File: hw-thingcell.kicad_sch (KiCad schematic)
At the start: 80 parts, among them J1 Conn_01x02_Pin, J2 GSM_ANT, J3 GNSS_ANT, J4 Conn_01x08_Pin, J5 SIM8060-6-0-14-00-A, K1 JRC-21F(4100), Q1 PMBT3904235, Q2 PMBT3904235, SW1 SW_Push, U1 ESP32-WROOM-32, U2 AP62301WU-7, U3 AP62301WU-7, U4 SIM868

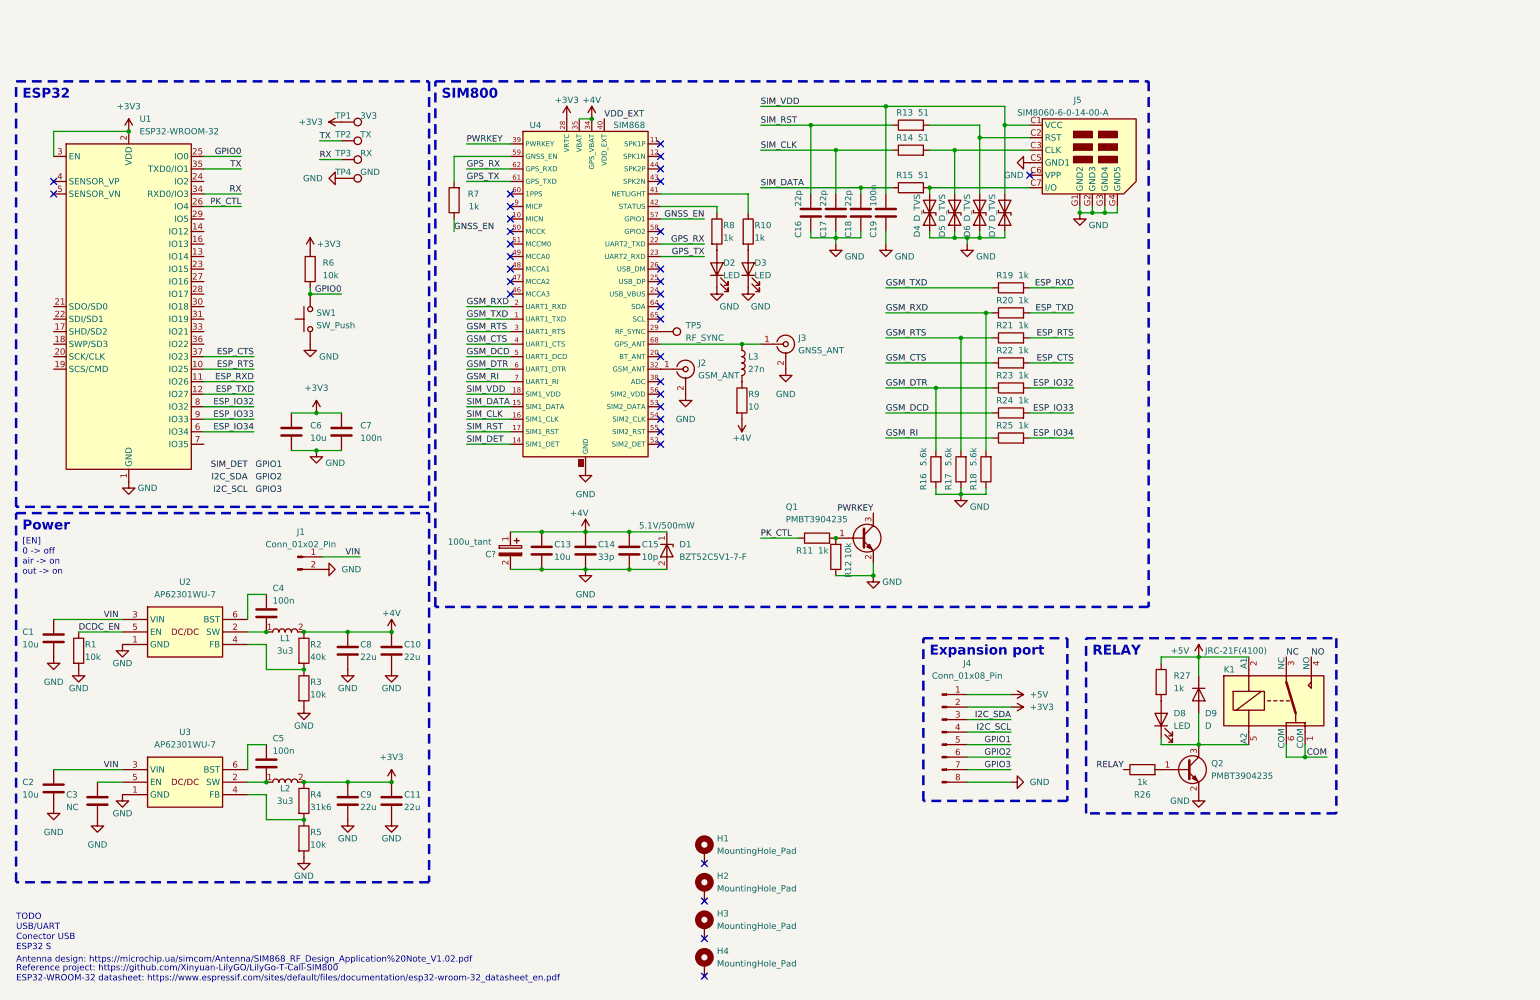
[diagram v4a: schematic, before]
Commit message: Add USB-UART and USB-C connector
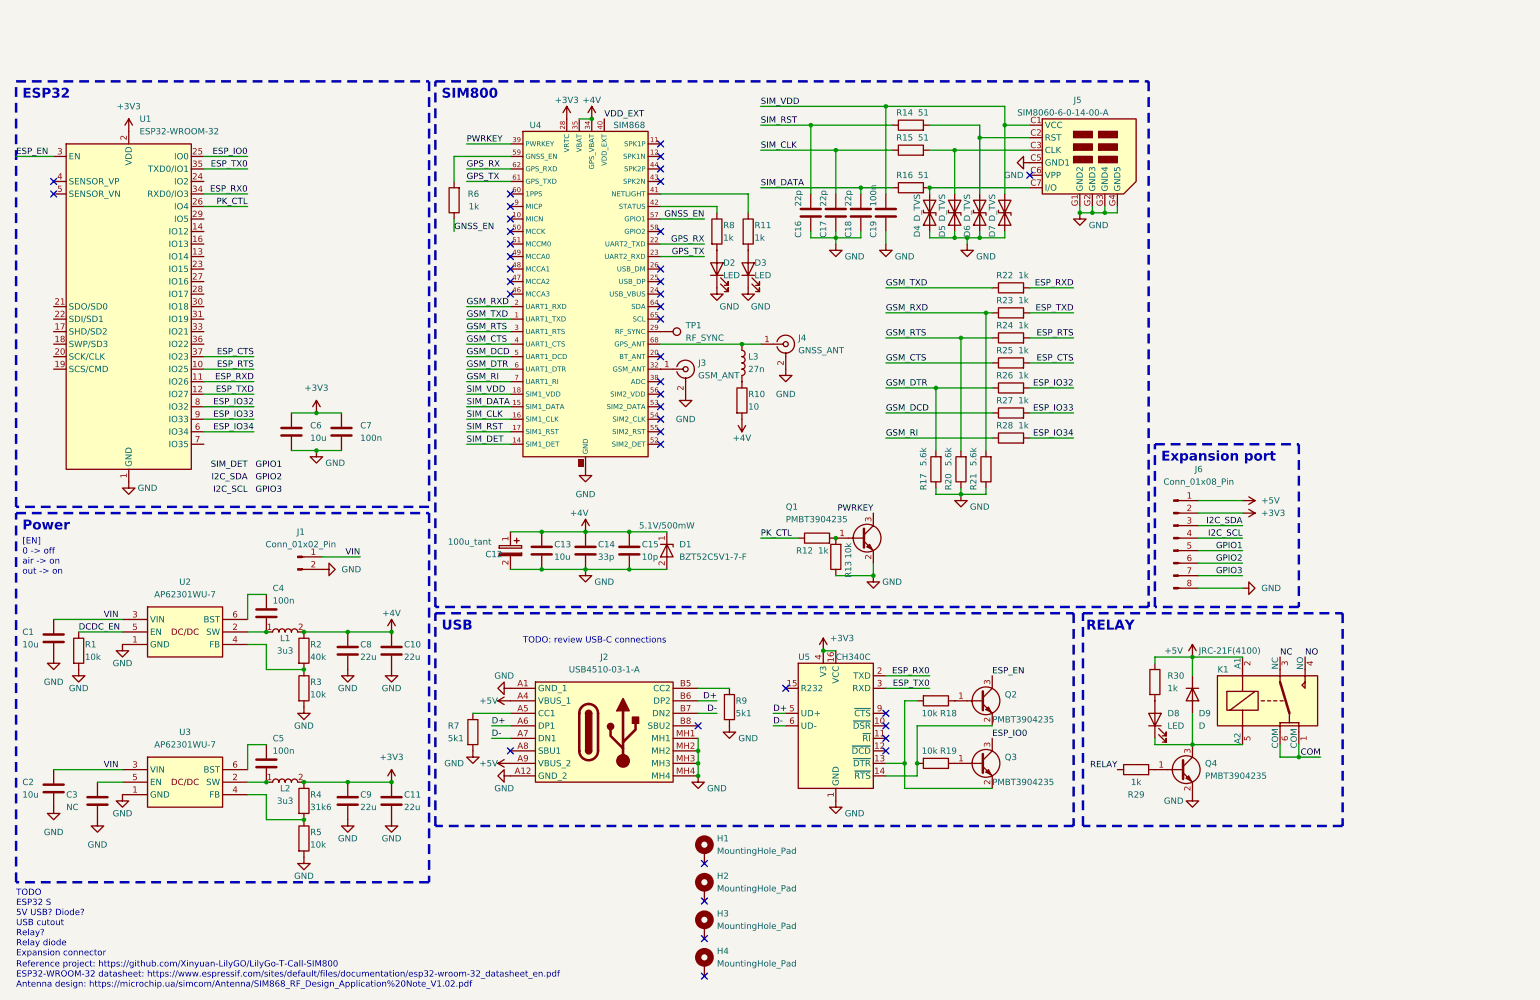
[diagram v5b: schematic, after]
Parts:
- removed R6: 10k, Resistor_SMD:R_0402_1005Metric, symbol Device:R
- removed SW1: SW_Push, symbol Switch:SW_Push
- removed TP1: 3V3, TestPoint:TestPoint_Pad_D1.0mm, symbol Connector:TestPoint
- removed TP2: TX, TestPoint:TestPoint_Pad_D1.0mm, symbol Connector:TestPoint
- removed TP3: RX, TestPoint:TestPoint_Pad_D1.0mm, symbol Connector:TestPoint
- removed TP4: GND, TestPoint:TestPoint_Pad_D1.0mm, symbol Connector:TestPoint
- added J2: USB4510-03-1-A, guille-lib:USB4510031A, symbol guille-lib:USB4510-03-1-A
- added Q2, Q3: PMBT3904235, Package_TO_SOT_SMD:SOT-23, symbol guille-lib:PMBT3904235
- added R18, R19: 10k, Resistor_SMD:R_0402_1005Metric, symbol Device:R
- added R7, R9: 5k1, Resistor_SMD:R_0402_1005Metric, symbol Device:R
- added U5: CH340C, Package_SO:SOIC-16_3.9x9.9mm_P1.27mm, symbol Interface_USB:CH340C
- gave numbers to parts that had none: 1
- renumbered J2 to J3, J3 to J4, J4 to J6, Q2 to Q4, R9 to R10, R10 to R11, R11 to R12, R12 to R13, R13 to R14, R14 to R15, R15 to R16, R16 to R17, R17 to R20, R18 to R21, R19 to R22, R20 to R23, R21 to R24, R22 to R25, R23 to R26, R24 to R27, R25 to R28, R26 to R29, R27 to R30, R7 to R6, TP5 to TP1
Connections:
- net +3V3: now also U5.16 (VCC), U5.4 (V3); no longer U1.3 (EN)
- net +5V: now also J2.A4 (VBUS_1), J2.A9 (VBUS_2)
- net GND: now also J2.A1 (GND_1), J2.A12 (GND_2), J2.MH1, J2.MH2, J2.MH3, J2.MH4, R7.2, R9.2, U5.1 (GND)
- net GPIO0 renamed ESP_IO0
- net ESP_IO0: now also Q3.3
- net RX renamed ESP_RX0
- net ESP_RX0: now also U5.2 (TXD)
- net TX renamed ESP_TX0
- net ESP_TX0: now also U5.3 (RXD)
- new net: Q3.2, R18.2, U5.13 (~{DTR})
- new net: Q2.2, R19.2, U5.14 (~{RTS})
- new net: Q2.1, R18.1
- new net: Q3.1, R19.1
- new net: J2.B5 (CC2), R9.1
- new net: J2.A5 (CC1), R7.1
- new net D+: J2.A6 (DP1), J2.B6 (DP2), U5.5 (UD+)
- new net D-: J2.A7 (DN1), J2.B7 (DN2), U5.6 (UD-)
- new net ESP_EN: Q2.3, U1.3 (EN)
- no-connect marks 33 -> 40
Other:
- note added: "Reference project: https://github.com/Xinyuan-LilyGO/LilyGo-T-Call-SIM800 ESP32-WROOM-32 datasheet: https://www.espressif.com/sites/default/files/documentation/esp32-wroom-32_datasheet_en.pdf Antenna design: https://microchip.ua/simcom/Antenna/SIM868_RF_Design_Application%20Note_V1.02.pdf"
- note added: "TODO ESP32 S 5V USB? Diode? USB cutout Relay? Relay diode Expansion connector"
- note added: "TODO: review USB-C connections"
- note added: "USB"
- note removed: "Antenna design: https://microchip.ua/simcom/Antenna/SIM868_RF_Design_Application%20Note_V1.02.pdf"
- note removed: "Reference project: https://github.com/Xinyuan-LilyGO/LilyGo-T-Call-SIM800 ESP32-WROOM-32 datasheet: https://www.espressif.com/sites/default/files/documentation/esp32-wroom-32_datasheet_en.pdf"
- note removed: "TODO USB/UART Conector USB ESP32 S"
- moved on the sheet: D8, D9, J6, K1, Q4, R29, R30

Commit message: Change ESP-WROOM to SOLO and schematic relocation
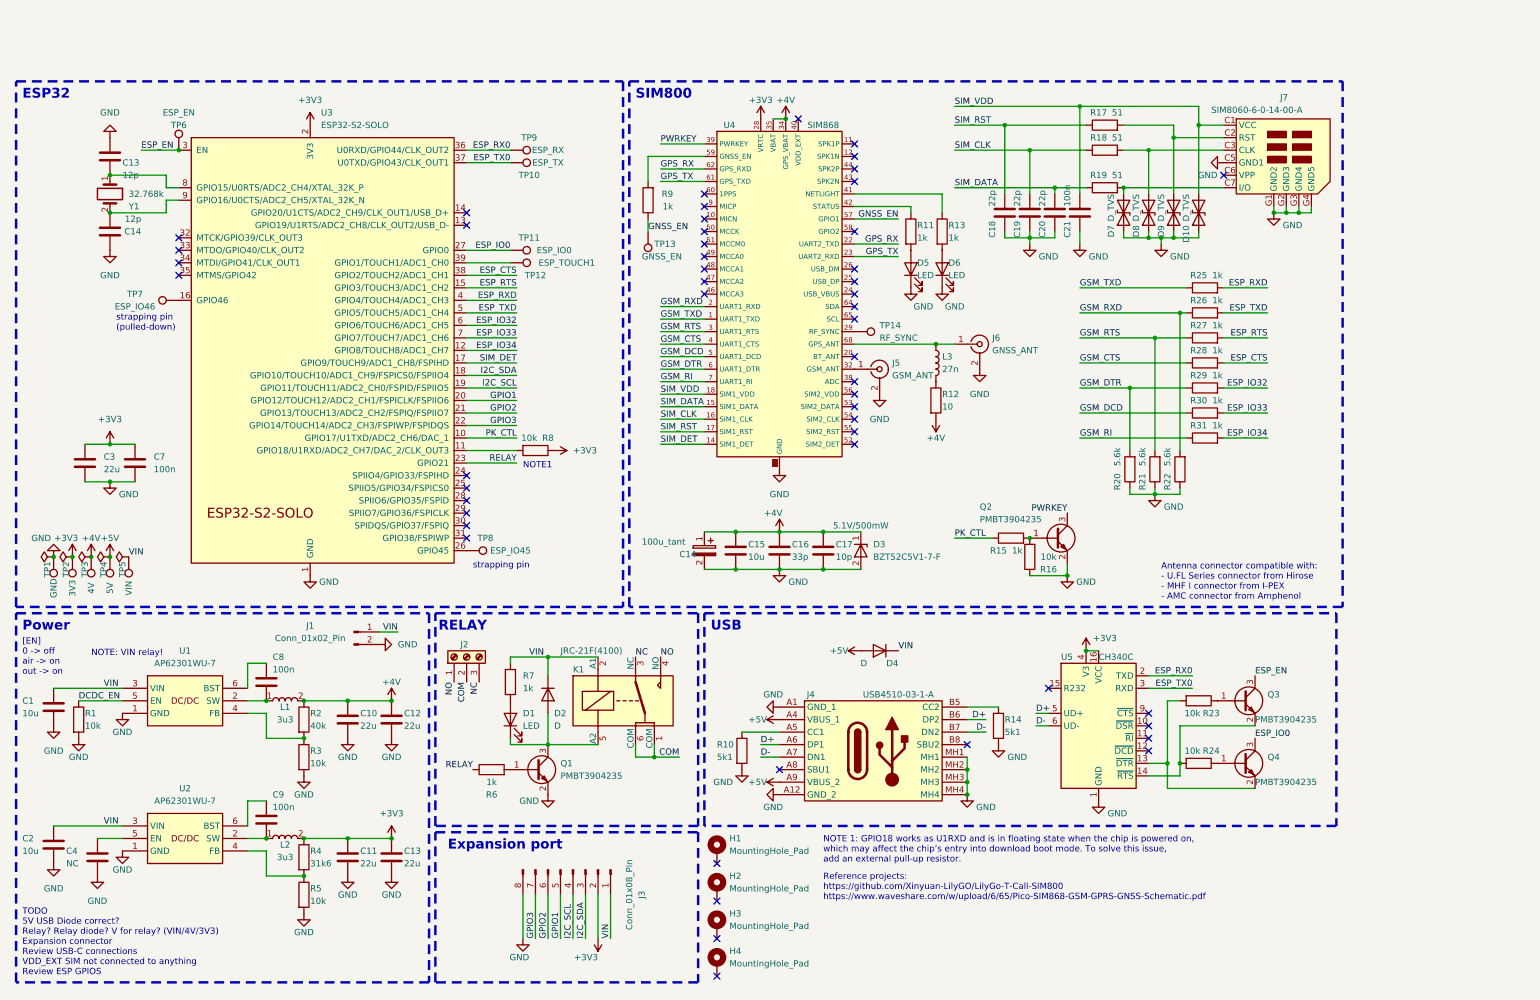
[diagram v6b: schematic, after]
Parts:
- removed U1: ESP32-WROOM-32, RF_Module:ESP32-WROOM-32, symbol RF_Module:ESP32-WROOM-32
- added C13, C14: 12p, Capacitor_SMD:C_0402_1005Metric, symbol Device:C
- added D4: D, symbol Device:D
- added J2: Screw_Terminal_01x03, symbol Connector:Screw_Terminal_01x03
- added R8: 10k, Resistor_SMD:R_0402_1005Metric, symbol Device:R
- added TP1: GND, TestPoint:TestPoint_Pad_D1.0mm, symbol Connector:TestPoint
- added TP10: ESP_TX, TestPoint:TestPoint_Pad_D1.0mm, symbol Connector:TestPoint
- added TP11: ESP_IO0, TestPoint:TestPoint_Pad_D1.0mm, symbol Connector:TestPoint
- added TP12: ESP_TOUCH1, TestPoint:TestPoint_Pad_D1.0mm, symbol Connector:TestPoint
- added TP13: GNSS_EN, TestPoint:TestPoint_Pad_D1.0mm, symbol Connector:TestPoint
- added TP2: 3V3, TestPoint:TestPoint_Pad_D1.0mm, symbol Connector:TestPoint
- added TP3: 4V, TestPoint:TestPoint_Pad_D1.0mm, symbol Connector:TestPoint
- added TP4: 5V, TestPoint:TestPoint_Pad_D1.0mm, symbol Connector:TestPoint
- added TP5: VIN, TestPoint:TestPoint_Pad_D1.0mm, symbol Connector:TestPoint
- added TP6: ESP_EN, TestPoint:TestPoint_Pad_D1.0mm, symbol Connector:TestPoint
- added TP7: ESP_IO46, TestPoint:TestPoint_Pad_D1.0mm, symbol Connector:TestPoint
- added TP8: ESP_IO45, TestPoint:TestPoint_Pad_D1.0mm, symbol Connector:TestPoint
- added TP9: ESP_RX, TestPoint:TestPoint_Pad_D1.0mm, symbol Connector:TestPoint
- added U3: ESP32-S2-SOLO, PCM_Espressif:ESP32-S2-SOLO, symbol guille-lib:ESP32-S2-SOLO
- added Y1: 32.768k, guille-lib:SC32S7PF20PPM, symbol guille-lib:SC32S-7PF20PPM
- C3: renamed from C6; value 10u -> 22u
- renumbered C8 to C10, C9 to C11, C10 to C12, C11 to C13, C12 to C14, C13 to C15, C14 to C16, C15 to C17, C16 to C18, C17 to C19, C18 to C20, C19 to C21, C3 to C4, C4 to C8, C5 to C9, D8 to D1, D7 to D10, D9 to D2, D1 to D3, D2 to D5, D3 to D6, D4 to D7, D5 to D8, D6 to D9, J6 to J3, J2 to J4, J3 to J5, J4 to J6, J5 to J7, Q4 to Q1, Q1 to Q2, Q2 to Q3, Q3 to Q4, R7 to R10, R8 to R11, R10 to R12, R11 to R13, R9 to R14, R12 to R15, R13 to R16, R14 to R17, R15 to R18, R16 to R19, R17 to R20, R20 to R21, R21 to R22, R18 to R23, R19 to R24, R22 to R25, R23 to R26, R24 to R27, R25 to R28, R26 to R29, R27 to R30, R28 to R31, R29 to R6, R30 to R7, R6 to R9, TP1 to TP14, U2 to U1, U3 to U2
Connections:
- net +3V3: now also R8.1, TP2.1, U3.2 (3V3)
- net +4V: now also TP3.1
- net +5V: now also D4.2 (A), TP4.1; no longer D2.1 (K), J3.1 (Pin_1), K1.2 (A1), R7.1
- net COM: now also J2.2 (Pin_2)
- net ESP_CTS: now also U3.38 (GPIO2/TOUCH2/ADC1_CH1)
- net ESP_EN: now also TP6.1, U3.3 (EN)
- net ESP_IO0: now also TP11.1, U3.27 (GPIO0)
- net ESP_IO32: now also U3.6 (GPIO6/TOUCH6/ADC1_CH5)
- net ESP_IO33: now also U3.7 (GPIO7/TOUCH7/ADC1_CH6)
- net ESP_IO34: now also U3.12 (GPIO8/TOUCH8/ADC1_CH7)
- net ESP_RTS: now also U3.15 (GPIO3/TOUCH3/ADC1_CH2)
- net ESP_RX0: now also TP9.1, U3.36 (U0RXD/GPIO44/CLK_OUT2)
- net ESP_RXD: now also U3.4 (GPIO4/TOUCH4/ADC1_CH3)
- net ESP_TX0: now also TP10.1, U3.37 (U0TXD/GPIO43/CLK_OUT1)
- net ESP_TXD: now also U3.5 (GPIO5/TOUCH5/ADC1_CH4)
- net GND: now also C13.1, C14.1, TP1.1, U3.1 (GND), U3.40 (GND), U3.41 (GND)
- net GNSS_EN: now also TP13.1
- net GPIO1: now also U3.20 (GPIO12/TOUCH12/ADC2_CH1/FSPICLK/FSPIIO6)
- net GPIO2: now also U3.21 (GPIO13/TOUCH13/ADC2_CH2/FSPIQ/FSPIIO7)
- net GPIO3: now also U3.22 (GPIO14/TOUCH14/ADC2_CH3/FSPIWP/FSPIDQS)
- net I2C_SCL: now also U3.19 (GPIO11/TOUCH11/ADC2_CH0/FSPID/FSPIIO5)
- net I2C_SDA: now also U3.18 (GPIO10/TOUCH10/ADC1_CH9/FSPICS0/FSPIIO4)
- net NC: now also J2.3 (Pin_3)
- net NO: now also J2.1 (Pin_1)
- net PK_CTL: now also U3.10 (GPIO17/U1TXD/ADC2_CH6/DAC_1)
- net RELAY: now also U3.23 (GPIO21)
- net SIM_DET: now also U3.17 (GPIO9/TOUCH9/ADC1_CH8/FSPIHD)
- net VIN: now also D2.1 (K), J3.1 (Pin_1), K1.2 (A1), R7.1, D4.1 (K), TP5.1
- net VDD_EXT: no longer names the net of U4.40 (VDD_EXT)
- new net: R8.2, U3.11 (GPIO18/U1RXD/ADC2_CH7/DAC_2/CLK_OUT3)
- new net: TP7.1, U3.16 (GPIO46)
- new net: TP8.1, U3.26 (GPIO45)
- new net: TP12.1, U3.39 (GPIO1/TOUCH1/ADC1_CH0)
- new net: C13.2, U3.8 (GPIO15/U0RTS/ADC2_CH4/XTAL_32K_P), Y1.1
- new net: C14.2, U3.9 (GPIO16/U0CTS/ADC2_CH5/XTAL_32K_N), Y1.2
- no-connect marks 40 -> 51
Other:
- note added: "Antenna connector compatible with: - U.FL Series connector from Hirose - MHF I connector from I-PEX - AMC connector from Amphenol"
- note added: "NOTE 1: GPIO18 works as U1RXD and is in floating state when the chip is powered on, which may affect the chip’s entry into download boot mode. To solve this issue, add an external pull-up resistor."
- note added: "NOTE1"
- note added: "NOTE: VIN relay!"
- note added: "Reference projects: https://github.com/Xinyuan-LilyGO/LilyGo-T-Call-SIM800 https://www.waveshare.com/w/upload/6/65/Pico-SIM868-GSM-GPRS-GNSS-Schematic.pdf"
- note added: "TODO 5V USB Diode correct? Relay? Relay diode? V for relay? (VIN/4V/3V3) Expansion connector Review USB-C connections VDD_EXT SIM not connected to anything Review ESP GPIOS"
- note added: "strapping pin"
- note added: "strapping pin (pulled-down)"
- note removed: "Reference project: https://github.com/Xinyuan-LilyGO/LilyGo-T-Call-SIM800 ESP32-WROOM-32 datasheet: https://www.espressif.com/sites/default/files/documentation/esp32-wroom-32_datasheet_en.pdf Antenna design: https://microchip.ua/simcom/Antenna/SIM868_RF_Design_Application%20Note_V1.02.pdf"
- note removed: "TODO ESP32 S 5V USB? Diode? USB cutout Relay? Relay diode Expansion connector"
- note removed: "TODO: review USB-C connections"
- moved on the sheet: C1, C10, C11, C12, C13, C14, C15, C16, C17, C18, C19, C2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

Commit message: Add supply diode and match all symbols&footprints
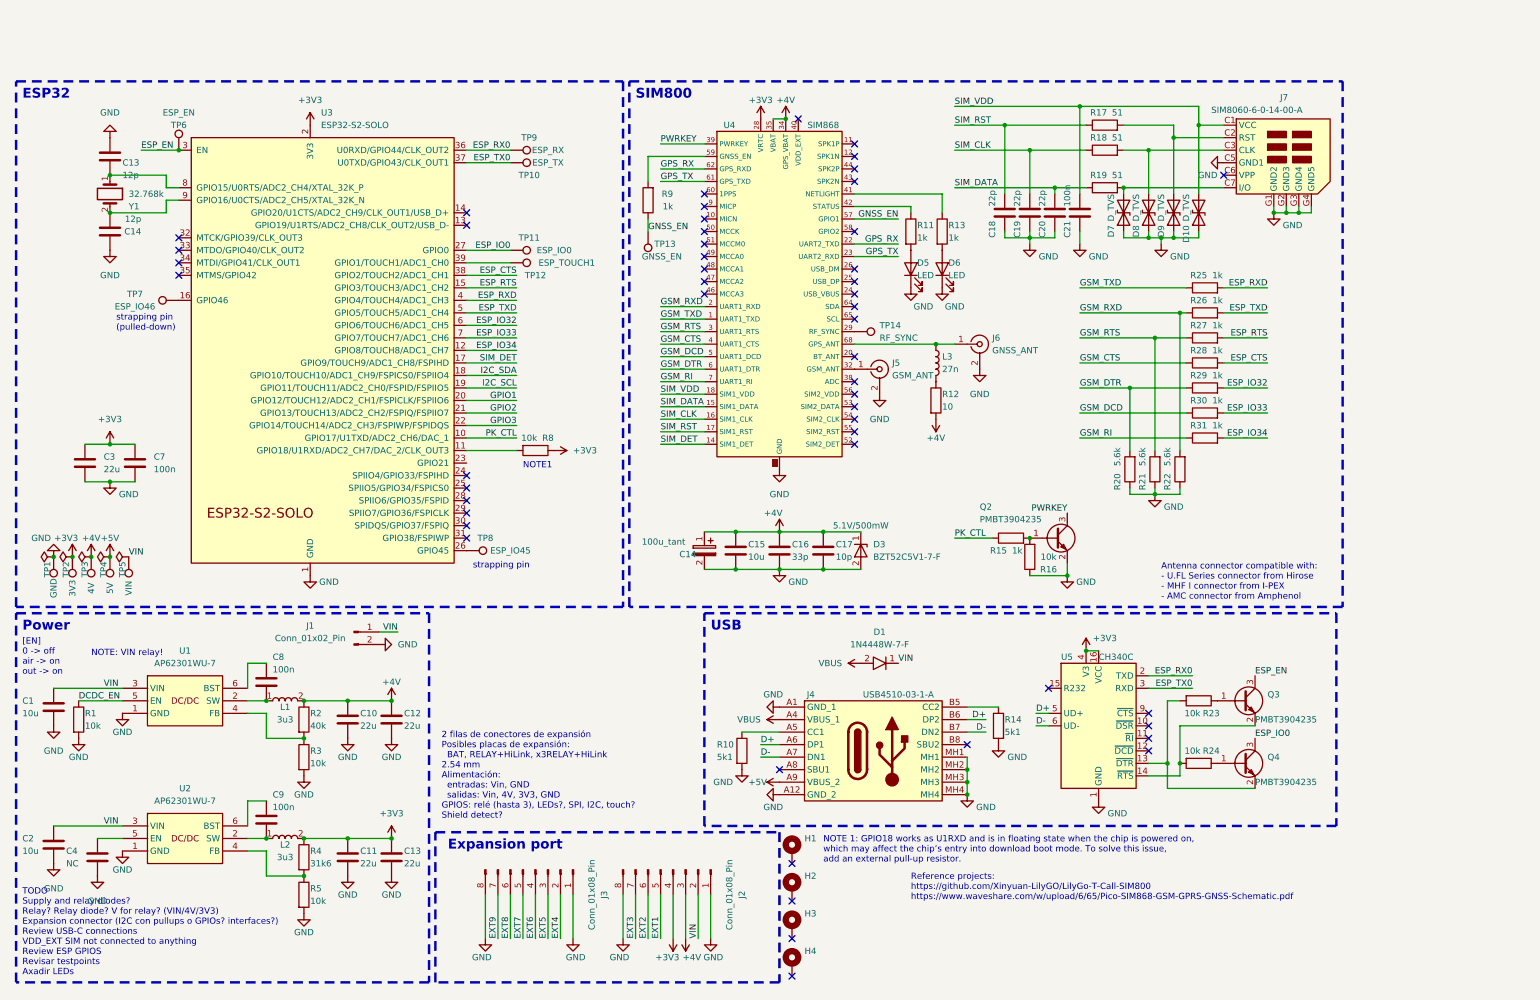
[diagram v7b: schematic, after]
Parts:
- removed D1: LED, LED_SMD:LED_0402_1005Metric, symbol Device:LED
- removed D2, D4: D, symbol Device:D
- removed J2: Screw_Terminal_01x03, symbol Connector:Screw_Terminal_01x03
- removed K1: JRC-21F(4100), guille-lib:JRC-21F(4100), symbol guille-lib:JRC-21F(4100)
- removed Q1: PMBT3904235, Package_TO_SOT_SMD:SOT-23, symbol guille-lib:PMBT3904235
- removed R6, R7: 1k, Resistor_SMD:R_0402_1005Metric, symbol Device:R
- added D1: 1N4448W-7-F, Diode_SMD:D_SOD-123, symbol guille-lib:1N4448W-7-F
- added J2: Conn_01x08_Pin, Connector_PinSocket_2.54mm:PinSocket_1x08_P2.54mm_Vertical, symbol Connector:Conn_01x08_Pin
- H1, H2, H3, H4: footprint MountingHole:MountingHole_2.2mm_M2_Pad -> MountingHole:MountingHole_2.2mm_M2_ISO7380_Pad
- J3: footprint (none) -> Connector_PinSocket_2.54mm:PinSocket_1x08_P2.54mm_Vertical
- J5, J6: Mouser (none) -> https://www.mouser.es/ProductDetail/TE-Connectivity-Linx-Te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
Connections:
- net +3V3: now also J2.4 (Pin_4); no longer J3.2 (Pin_2)
- net +4V: now also J2.3 (Pin_3)
- net +5V: no longer J4.A4 (VBUS_1)
- net GND: now also J3.1 (Pin_1), J2.1 (Pin_1), J2.8 (Pin_8)
- net GPIO1: no longer J3.5 (Pin_5)
- net GPIO2: no longer J3.6 (Pin_6)
- net GPIO3: no longer J3.7 (Pin_7)
- net I2C_SCL: no longer J3.4 (Pin_4)
- net I2C_SDA: no longer J3.3 (Pin_3)
- net VIN: now also D1.1, J2.2 (Pin_2); no longer J3.1 (Pin_1)
- net RELAY: no longer names the net of U3.23 (GPIO21)
- new net EXT1: J2.5 (Pin_5)
- new net EXT2: J2.6 (Pin_6)
- new net EXT3: J2.7 (Pin_7)
- new net EXT4: J3.2 (Pin_2)
- new net EXT5: J3.3 (Pin_3)
- new net EXT6: J3.4 (Pin_4)
- new net EXT7: J3.5 (Pin_5)
- new net EXT8: J3.6 (Pin_6)
- new net EXT9: J3.7 (Pin_7)
- new net VBUS: D1.2, J4.A4 (VBUS_1)
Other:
- note added: "2 filas de conectores de expansión Posibles placas de expansión: BAT, RELAY+HiLink, x3RELAY+HiLink 2.54 mm Alimentación: entradas: Vin, GND salidas: Vin, 4V, 3V3, GND GPIOS: relé (hasta 3), LEDs?, SPI, I2C, touch? Shield detect?"
- note added: "TODO Supply and relay diodes? Relay? Relay diode? V for relay? (VIN/4V/3V3) Expansion connector (I2C con pullups o GPIOs? interfaces?) Review USB-C connections VDD_EXT SIM not connected to anything Review ESP GPIOS Revisar testpoints Axadir LEDs"
- note removed: "RELAY"
- note removed: "TODO 5V USB Diode correct? Relay? Relay diode? V for relay? (VIN/4V/3V3) Expansion connector Review USB-C connections VDD_EXT SIM not connected to anything Review ESP GPIOS"
- moved on the sheet: H1, H2, H3, H4, J3
